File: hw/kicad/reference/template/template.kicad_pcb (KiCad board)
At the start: 2 copper layers, 40 x 40 mm, 2 parts, among them J1 TOP, J2 BUTTOM

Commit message: Merge from normal
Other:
- board size 40 x 40 mm -> 45 x 45 mm
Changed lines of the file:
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@@
     )
     (pad_to_mask_clearance 0)
-    (grid_origin 55.72 75.22)
+    (grid_origin 53.22 75.22)
     (pcbplotparams
       (layerselection 0x00010fc_ffffffff)
@@
     )
   )
-  (gr_line locked (start 93.22 75.22) (end 93.22 40.22)
+  (gr_line locked (start 95.72 75.22) (end 95.72 35.22)
     (stroke (width 0.1) (type default)) (layer "Edge.Cuts"))
-  (gr_arc locked (start 53.22 40.22) (mid 53.952233 38.452233) (end 55.72 37.72)
+  (gr_arc locked (start 50.72 35.22) (mid 51.452233 33.452233) (end 53.22 32.72)
     (stroke (width 0.1) (type default)) (layer "Edge.Cuts"))
-  (gr_circle locked (center 90.72 75.22) (end 89.22 75.22)
+  (gr_circle locked (center 93.22 75.22) (end 91.72 75.22)
     (stroke (width 0.1) (type default)) (fill none) (layer "Edge.Cuts"))
-  (gr_circle locked (center 55.72 40.22) (end 57.22 40.22)
+  (gr_circle locked (center 53.22 35.22) (end 54.72 35.22)
     (stroke (width 0.1) (type default)) (fill none) (layer "Edge.Cuts"))
-  (gr_line locked (start 90.72 37.72) (end 55.72 37.72)
+  (gr_line locked (start 93.22 32.72) (end 53.22 32.72)
     (stroke (width 0.1) (type default)) (layer "Edge.Cuts"))
-  (gr_arc locked (start 90.72 37.72) (mid 92.487767 38.452233) (end 93.22 40.22)
+  (gr_arc locked (start 93.22 32.72) (mid 94.987767 33.452233) (end 95.72 35.22)
     (stroke (width 0.1) (type default)) (layer "Edge.Cuts"))
-  (gr_arc locked (start 93.22 75.22) (mid 92.487767 76.987767) (end 90.72 77.72)
+  (gr_arc locked (start 95.72 75.22) (mid 94.987767 76.987767) (end 93.22 77.72)
     (stroke (width 0.1) (type default)) (layer "Edge.Cuts"))
-  (gr_circle locked (center 90.72 40.22) (end 90.72 41.72)
+  (gr_circle locked (center 93.22 35.22) (end 93.22 36.72)
     (stroke (width 0.1) (type default)) (fill none) (layer "Edge.Cuts"))
-  (gr_line locked (start 55.72 77.72) (end 90.72 77.72)
+  (gr_line locked (start 53.22 77.72) (end 93.22 77.72)
     (stroke (width 0.1) (type default)) (layer "Edge.Cuts"))
-  (gr_arc locked (start 55.72 77.72) (mid 53.952233 76.987767) (end 53.22 75.22)
+  (gr_arc locked (start 53.22 77.72) (mid 51.452233 76.987767) (end 50.72 75.22)
     (stroke (width 0.1) (type default)) (layer "Edge.Cuts"))
-  (gr_circle locked (center 55.72 75.22) (end 55.72 73.72)
+  (gr_circle locked (center 53.22 75.22) (end 53.22 73.72)
     (stroke (width 0.1) (type default)) (fill none) (layer "Edge.Cuts"))
-  (gr_line locked (start 53.22 40.22) (end 53.22 75.22)
+  (gr_line locked (start 50.72 35.22) (end 50.72 75.22)
     (stroke (width 0.1) (type default)) (layer "Edge.Cuts"))
   (segment (start 77.665 70.27) (end 77.665 74.17) (width 0.762) (layer "F.Cu") (net 1))
@@
     (connect_pads yes (clearance 0.1524))
     (min_thickness 0.1524) (filled_areas_thickness no)
-    (fill (thermal_gap 0.1524) (thermal_bridge_width 0.1524) (smoothing fillet) (radius 0.1524))
+    (fill yes (thermal_gap 0.1524) (thermal_bridge_width 0.1524) (smoothing fillet) (radius 0.1524))
     (polygon
       (pts
-        (xy 50.165 37.0078)
-        (xy 94.1756 37.0184)
-        (xy 94.2264 78.5474)
+        (xy 50.038 32.004)
+        (xy 96.012 32.004)
+        (xy 96.012 78.232)
         (xy 50.038 78.232)
       )

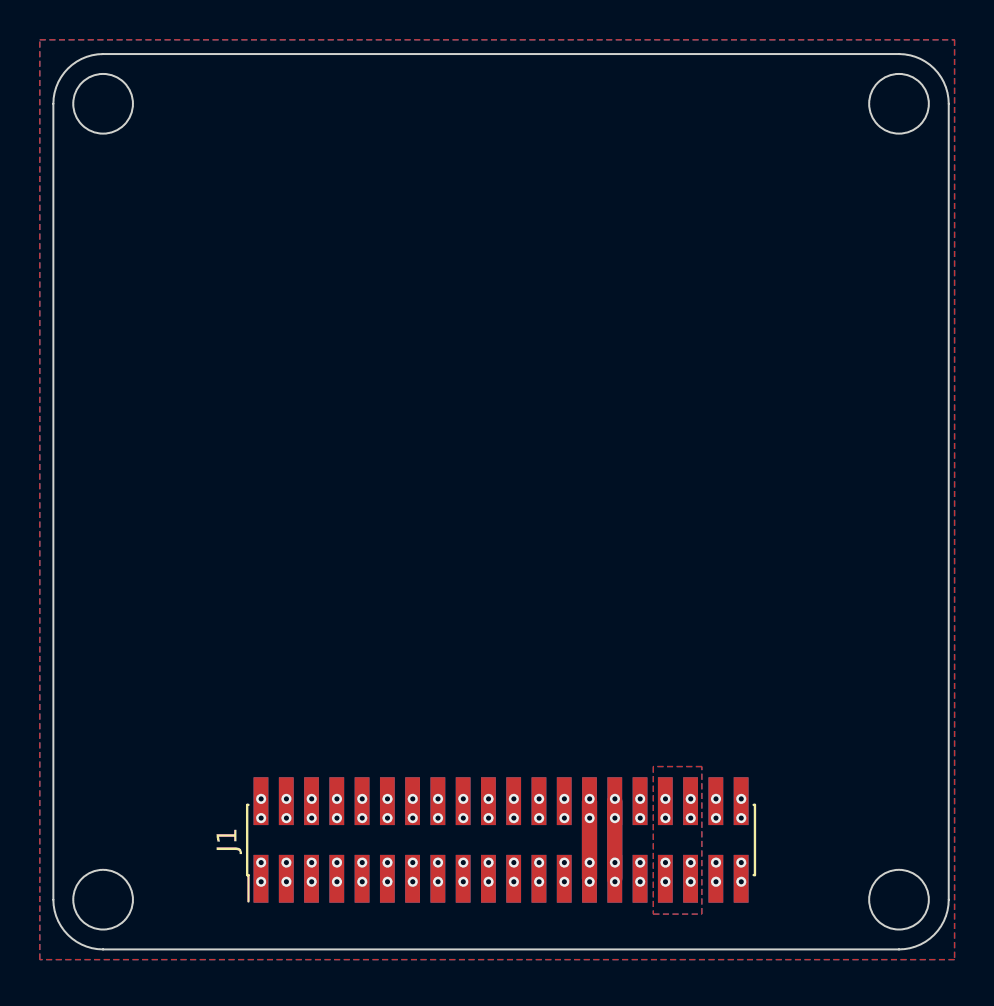
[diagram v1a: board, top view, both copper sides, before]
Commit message: 尽力改成40mmx40mm
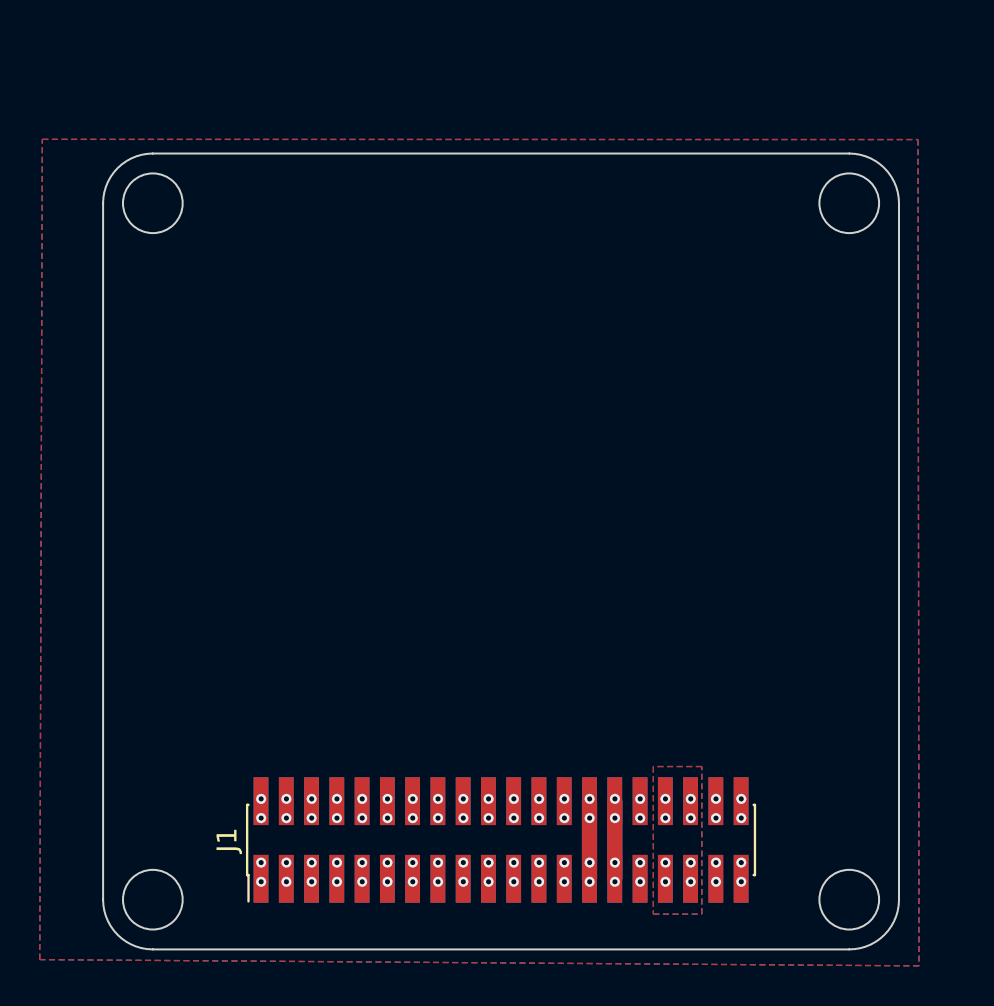
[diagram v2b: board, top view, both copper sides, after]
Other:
- board size 45 x 45 mm -> 40 x 40 mm
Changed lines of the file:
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@@
     )
     (pad_to_mask_clearance 0)
-    (grid_origin 53.22 75.22)
+    (grid_origin 55.72 75.22)
     (pcbplotparams
       (layerselection 0x00010fc_ffffffff)
@@
     )
   )
-  (gr_line locked (start 95.72 75.22) (end 95.72 35.22)
+  (gr_line locked (start 93.22 75.22) (end 93.22 40.22)
     (stroke (width 0.1) (type default)) (layer "Edge.Cuts"))
-  (gr_arc locked (start 50.72 35.22) (mid 51.452233 33.452233) (end 53.22 32.72)
+  (gr_arc locked (start 53.22 40.22) (mid 53.952233 38.452233) (end 55.72 37.72)
     (stroke (width 0.1) (type default)) (layer "Edge.Cuts"))
-  (gr_circle locked (center 93.22 75.22) (end 91.72 75.22)
+  (gr_circle locked (center 90.72 75.22) (end 89.22 75.22)
     (stroke (width 0.1) (type default)) (fill none) (layer "Edge.Cuts"))
-  (gr_circle locked (center 53.22 35.22) (end 54.72 35.22)
+  (gr_circle locked (center 55.72 40.22) (end 57.22 40.22)
     (stroke (width 0.1) (type default)) (fill none) (layer "Edge.Cuts"))
-  (gr_line locked (start 93.22 32.72) (end 53.22 32.72)
+  (gr_line locked (start 90.72 37.72) (end 55.72 37.72)
     (stroke (width 0.1) (type default)) (layer "Edge.Cuts"))
-  (gr_arc locked (start 93.22 32.72) (mid 94.987767 33.452233) (end 95.72 35.22)
+  (gr_arc locked (start 90.72 37.72) (mid 92.487767 38.452233) (end 93.22 40.22)
     (stroke (width 0.1) (type default)) (layer "Edge.Cuts"))
-  (gr_arc locked (start 95.72 75.22) (mid 94.987767 76.987767) (end 93.22 77.72)
+  (gr_arc locked (start 93.22 75.22) (mid 92.487767 76.987767) (end 90.72 77.72)
     (stroke (width 0.1) (type default)) (layer "Edge.Cuts"))
-  (gr_circle locked (center 93.22 35.22) (end 93.22 36.72)
+  (gr_circle locked (center 90.72 40.22) (end 90.72 41.72)
     (stroke (width 0.1) (type default)) (fill none) (layer "Edge.Cuts"))
-  (gr_line locked (start 53.22 77.72) (end 93.22 77.72)
+  (gr_line locked (start 55.72 77.72) (end 90.72 77.72)
     (stroke (width 0.1) (type default)) (layer "Edge.Cuts"))
-  (gr_arc locked (start 53.22 77.72) (mid 51.452233 76.987767) (end 50.72 75.22)
+  (gr_arc locked (start 55.72 77.72) (mid 53.952233 76.987767) (end 53.22 75.22)
     (stroke (width 0.1) (type default)) (layer "Edge.Cuts"))
-  (gr_circle locked (center 53.22 75.22) (end 53.22 73.72)
+  (gr_circle locked (center 55.72 75.22) (end 55.72 73.72)
     (stroke (width 0.1) (type default)) (fill none) (layer "Edge.Cuts"))
-  (gr_line locked (start 50.72 35.22) (end 50.72 75.22)
+  (gr_line locked (start 53.22 40.22) (end 53.22 75.22)
     (stroke (width 0.1) (type default)) (layer "Edge.Cuts"))
   (segment (start 77.665 70.27) (end 77.665 74.17) (width 0.762) (layer "F.Cu") (net 1))
@@
     (connect_pads yes (clearance 0.1524))
     (min_thickness 0.1524) (filled_areas_thickness no)
-    (fill yes (thermal_gap 0.1524) (thermal_bridge_width 0.1524) (smoothing fillet) (radius 0.1524))
+    (fill (thermal_gap 0.1524) (thermal_bridge_width 0.1524) (smoothing fillet) (radius 0.1524))
     (polygon
       (pts
-        (xy 50.038 32.004)
-        (xy 96.012 32.004)
-        (xy 96.012 78.232)
+        (xy 50.165 37.0078)
+        (xy 94.1756 37.0184)
+        (xy 94.2264 78.5474)
         (xy 50.038 78.232)
       )
